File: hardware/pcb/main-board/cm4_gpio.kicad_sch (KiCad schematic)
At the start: 14 parts, among them J402 CM4Lite SD Card, U402 RT9742SNGV

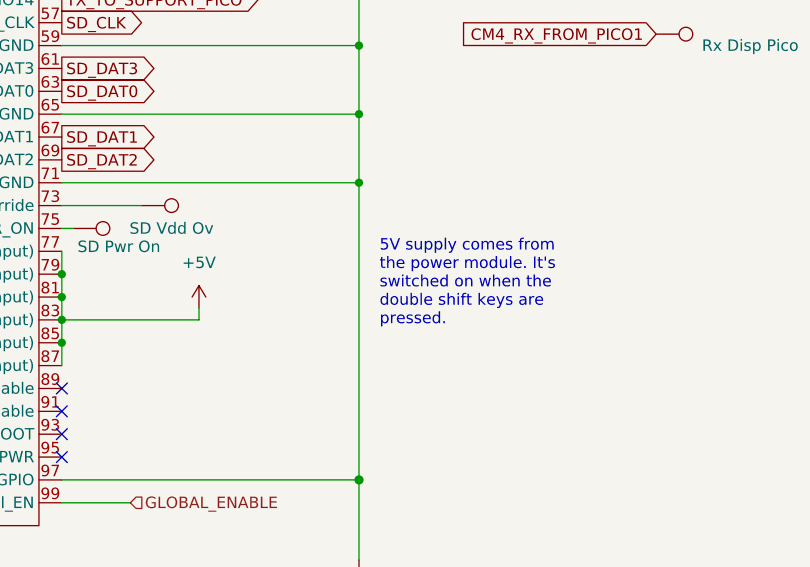
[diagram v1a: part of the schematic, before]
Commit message: CM4 power switch
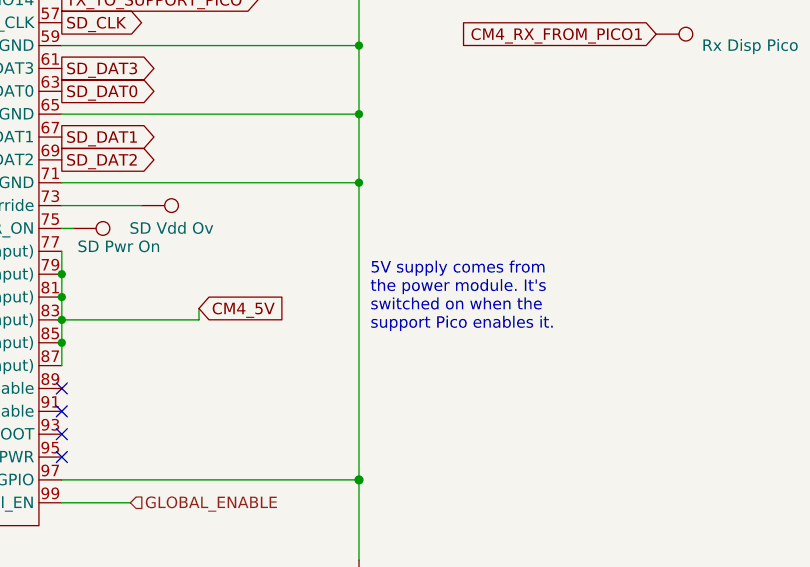
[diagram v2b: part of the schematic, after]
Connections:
- net +5V: no longer Module301.77 (+5v_(Input)), Module301.79 (+5v_(Input)), Module301.81 (+5v_(Input)), Module301.83 (+5v_(Input)), Module301.85 (+5v_(Input)), Module301.87 (+5v_(Input))
- new net CM4_5V: Module301.77 (+5v_(Input)), Module301.79 (+5v_(Input)), Module301.81 (+5v_(Input)), Module301.83 (+5v_(Input)), Module301.85 (+5v_(Input)), Module301.87 (+5v_(Input))
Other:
- note added: "5V supply comes from the power module. It's switched on when the support Pico enables it."
- note removed: "5V supply comes from the power module. It's switched on when the double shift keys are pressed."
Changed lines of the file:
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@@
 		)
 	)
-	(text "5V supply comes from\nthe power module. It's\nswitched on when the\ndouble shift keys are\npressed."
+	(text "5V supply comes from\nthe power module. It's\nswitched on when the\nsupport Pico enables it."
 		(exclude_from_sim no)
-		(at 141.986 130.556 0)
+		(at 140.97 132.08 0)
 		(effects
 			(font
@@
 		(property "Intersheetrefs" "${INTERSHEET_REFS}"
 			(at 120.9853 68.58 0)
+			(effects
+				(font
+					(size 1.27 1.27)
+				)
+				(justify left)
+				(hide yes)
+			)
+		)
+	)
+	(global_label "CM4_5V"
+		(shape input)
+		(at 121.92 133.35 0)
+		(fields_autoplaced yes)
+		(effects
+			(font
+				(size 1.27 1.27)
+			)
+			(justify left)
+		)
+		(property "Intersheetrefs" "${INTERSHEET_REFS}"
+			(at 131.4476 133.35 0)
 			(effects
 				(font
@@
 					(unit 1)
 				)
-			)
-		)
-	)
-	(symbol
-		(lib_id "power:+5V")
-		(at 121.92 133.35 0)
-		(unit 1)
-		(exclude_from_sim no)
-		(in_bom yes)
-		(on_board yes)
-		(dnp no)
-		(fields_autoplaced yes)
-		(property "Reference" "#PWR0402"
-			(at 121.92 137.16 0)
-			(effects
-				(font
-					(size 1.27 1.27)
-				)
-				(hide yes)
-			)
-		)
-		(property "Value" "+5V"
-			(at 121.92 128.27 0)
-			(effects
-				(font
-					(size 1.27 1.27)
-				)
-			)
-		)
-		(property "Footprint" ""
-			(at 121.92 133.35 0)
-			(effects
-				(font
-					(size 1.27 1.27)
-				)
-				(hide yes)
-			)
-		)
-		(property "Datasheet" ""
-			(at 121.92 133.35 0)
-			(effects
-				(font
-					(size 1.27 1.27)
-				)
-				(hide yes)
-			)
-		)
-		(property "Description" "Power symbol creates a global label with name \"+5V\""
-			(at 121.92 133.35 0)
-			(effects
-				(font
-					(size 1.27 1.27)
-				)
-				(hide yes)
-			)
-		)
-		(pin "1"
-		)
-		(instances
-			(project ""
-				(path "/fdce8012-5f35-4f58-8abb-80214b4af8fe/cd15a5fd-9317-456a-844b-3d9269d12c2d"
-					(reference "#PWR0402")
-					(unit 1)
-				)

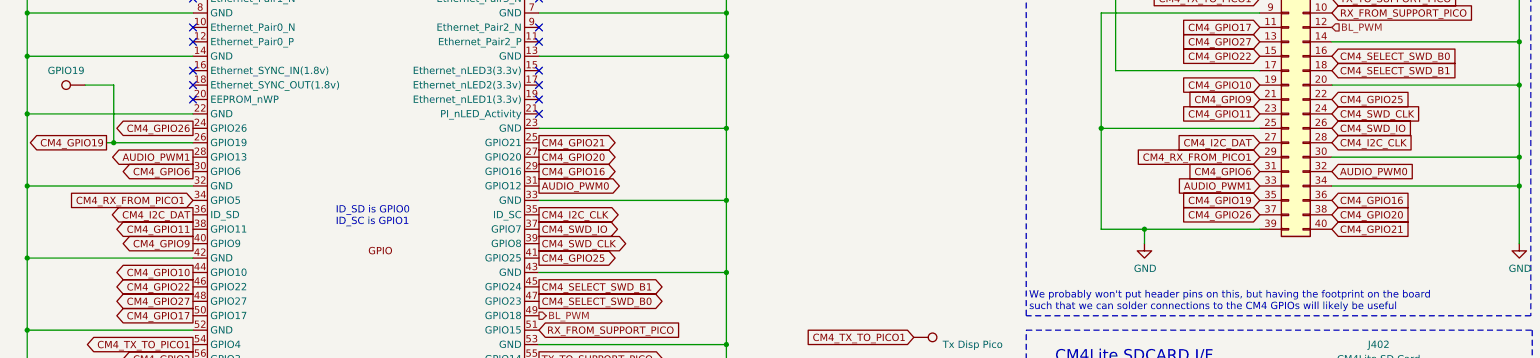
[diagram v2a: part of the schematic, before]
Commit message: add i2c connection to the support pico so it can control the RTC
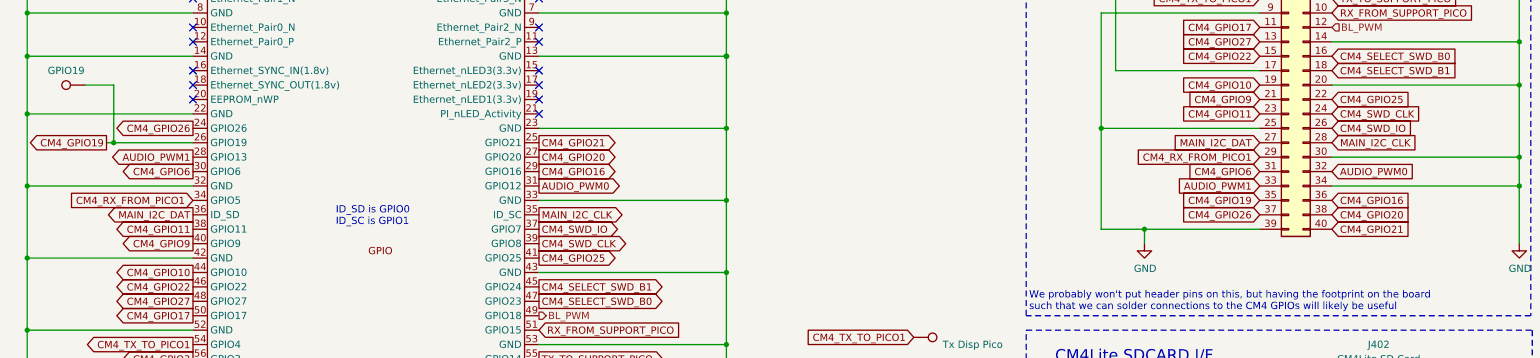
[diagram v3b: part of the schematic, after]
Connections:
- net CM4_I2C_CLK renamed MAIN_I2C_CLK
- net CM4_I2C_DAT renamed MAIN_I2C_DAT
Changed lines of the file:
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@@
 		)
 	)
-	(global_label "CM4_I2C_CLK"
+	(global_label "MAIN_I2C_CLK"
 		(shape input)
 		(at 246.38 60.96 0)
@@
 		)
 		(property "Intersheetrefs" "${INTERSHEET_REFS}"
-			(at 261.2295 60.96 0)
+			(at 261.7739 60.96 0)
 			(effects
 				(font
@@
 		)
 	)
-	(global_label "CM4_I2C_CLK"
+	(global_label "MAIN_I2C_CLK"
 		(shape output)
 		(at 106.68 73.66 0)
@@
 		)
 		(property "Intersheetrefs" "${INTERSHEET_REFS}"
-			(at 121.5295 73.66 0)
-			(effects
-				(font
-					(size 1.27 1.27)
-				)
-				(justify left)
-				(hide yes)
-			)
-		)
-	)
-	(global_label "CM4_I2C_DAT"
+			(at 122.0739 73.66 0)
+			(effects
+				(font
+					(size 1.27 1.27)
+				)
+				(justify left)
+				(hide yes)
+			)
+		)
+	)
+	(global_label "MAIN_I2C_DAT"
 		(shape output)
 		(at 45.72 73.66 180)
@@
 		)
 		(property "Intersheetrefs" "${INTERSHEET_REFS}"
-			(at 31.1124 73.66 0)
+			(at 30.568 73.66 0)
 			(effects
 				(font
@@
 		)
 	)
-	(global_label "CM4_I2C_DAT"
+	(global_label "MAIN_I2C_DAT"
 		(shape input)
 		(at 233.68 60.96 180)
@@
 		)
 		(property "Intersheetrefs" "${INTERSHEET_REFS}"
-			(at 219.0724 60.96 0)
-			(effects
-				(font
+			(at 218.528 60.96 0)
+			(effects
+				(font

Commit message: make a start on RP2040 to replace the KB pico
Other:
- title: Z88R - Z88 Recreated -> Z88R - Z88 Recreation
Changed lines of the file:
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@@
 	(paper "A4")
 	(title_block
-		(title "Z88R - Z88 Recreated")
-		(date "2025-12-19")
-		(rev "20251219WIP")
+		(title "Z88R - Z88 Recreation")
+		(date "2025-12-30")
+		(rev "20251230WIP")
 		(company "Fountain and Menadue")
 	)

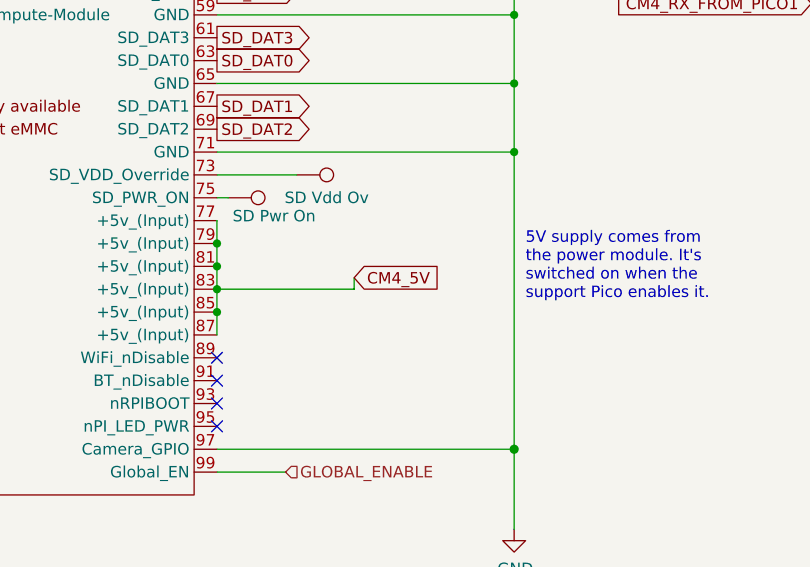
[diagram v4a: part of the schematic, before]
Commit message: start the support pico rp2040 replacement
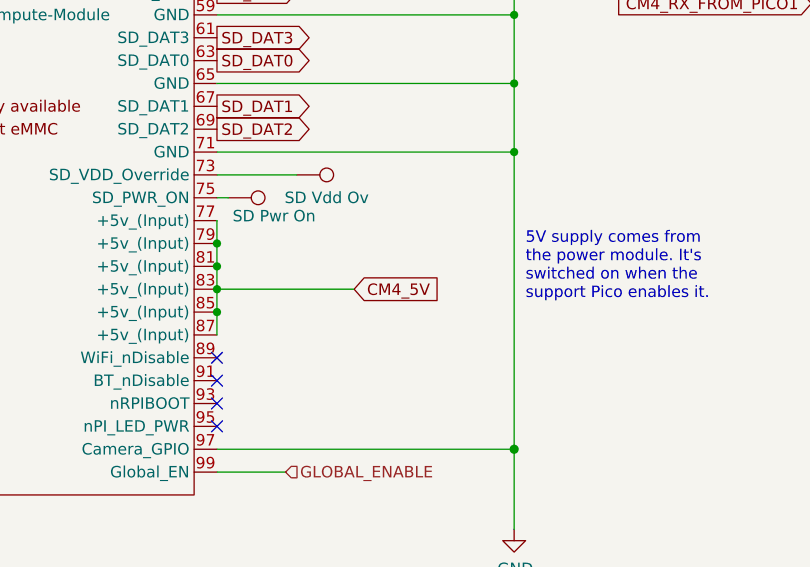
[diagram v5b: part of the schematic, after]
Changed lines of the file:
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@@
 	(title_block
 		(title "Z88R - Z88 Recreation")
-		(date "2025-12-30")
-		(rev "20251230WIP")
+		(date "2026-01-01")
+		(rev "20260101WIP")
 		(company "Fountain and Menadue")
 	)
@@
 			(width 0)
 			(type solid)
-		)
-	)
-	(wire
-		(pts
-			(xy 121.92 134.62) (xy 121.92 133.35)
-		)
-		(stroke
-			(width 0)
-			(type default)
 		)
 	)
@@
 	(global_label "CM4_5V"
 		(shape input)
-		(at 121.92 133.35 0)
+		(at 121.92 134.62 0)
 		(fields_autoplaced yes)
 		(effects
@@
 		)
 		(property "Intersheetrefs" "${INTERSHEET_REFS}"
-			(at 131.4476 133.35 0)
+			(at 131.4476 134.62 0)
 			(effects
 				(font

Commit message: more support rp2040 cleanups
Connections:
- net RX_FROM_SUPPORT_PICO renamed RX_FROM_SP_RP
- net TX_TO_SUPPORT_PICO renamed TX_TO_SP_RP
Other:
- note added: "5V supply comes from the power module. It's switched on when the support RP2040 enables it."
- note removed: "5V supply comes from the power module. It's switched on when the support Pico enables it."
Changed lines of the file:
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@@
 		)
 	)
-	(text "5V supply comes from\nthe power module. It's\nswitched on when the\nsupport Pico enables it."
+	(text "5V supply comes from\nthe power module. It's\nswitched on when the\nsupport RP2040 enables it."
 		(exclude_from_sim no)
 		(at 140.97 132.08 0)
@@
 		)
 	)
-	(global_label "RX_FROM_SUPPORT_PICO"
+	(global_label "RX_FROM_SP_RP"
 		(shape input)
 		(at 106.68 93.98 0)
@@
 		)
 		(property "Intersheetrefs" "${INTERSHEET_REFS}"
-			(at 132.6572 93.98 0)
+			(at 124.5533 93.98 0)
 			(effects
 				(font
@@
 		)
 	)
-	(global_label "RX_FROM_SUPPORT_PICO"
+	(global_label "RX_FROM_SP_RP"
 		(shape input)
 		(at 246.38 38.1 0)
@@
 		)
 		(property "Intersheetrefs" "${INTERSHEET_REFS}"
-			(at 272.3572 38.1 0)
+			(at 264.2533 38.1 0)
 			(effects
 				(font
@@
 		)
 	)
-	(global_label "TX_TO_SUPPORT_PICO"
+	(global_label "TX_TO_SP_RP"
 		(shape input)
 		(at 246.38 35.56 0)
@@
 		)
 		(property "Intersheetrefs" "${INTERSHEET_REFS}"
-			(at 269.2124 35.56 0)
+			(at 261.1085 35.56 0)
 			(effects
 				(font
@@
 		)
 	)
-	(global_label "TX_TO_SUPPORT_PICO"
+	(global_label "TX_TO_SP_RP"
 		(shape output)
 		(at 106.68 99.06 0)
@@
 		)
 		(property "Intersheetrefs" "${INTERSHEET_REFS}"
-			(at 129.5124 99.06 0)
-			(effects
-				(font
+			(at 121.4085 99.06 0)
+			(effects
+				(font

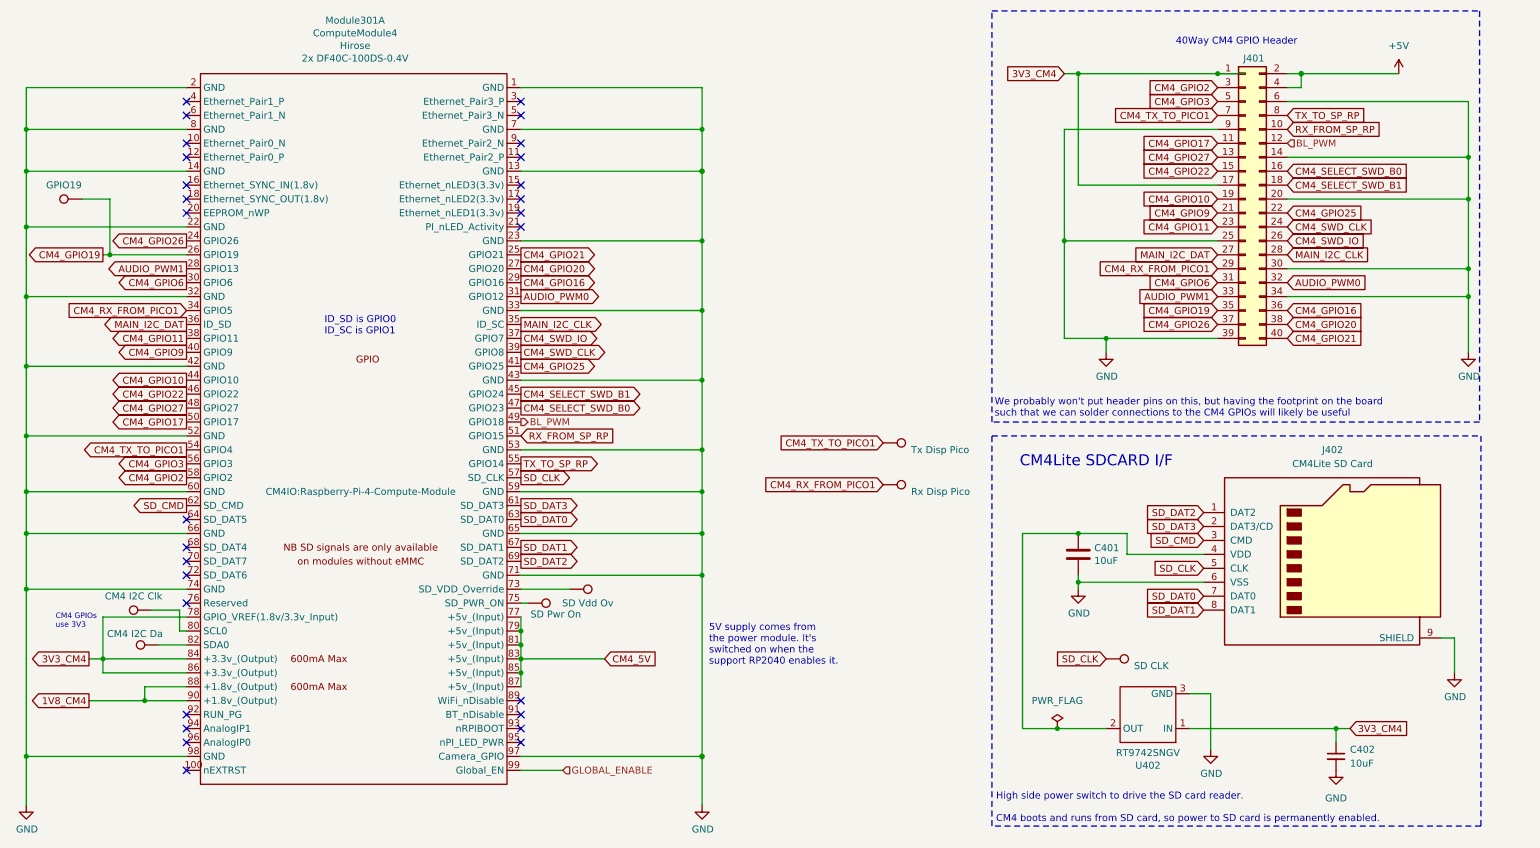
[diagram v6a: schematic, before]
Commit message: rename display board things to application board things
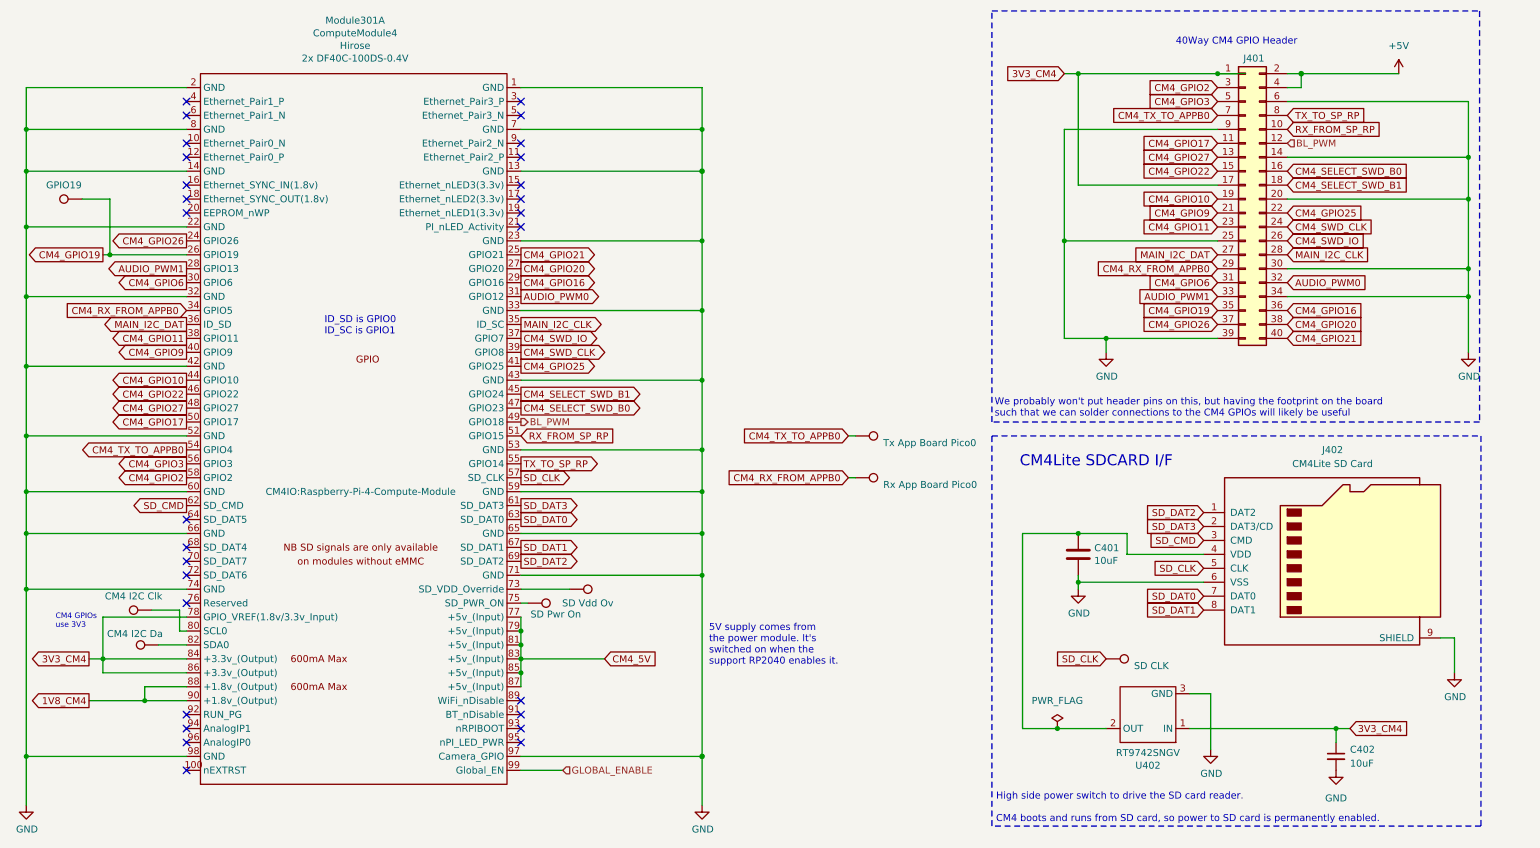
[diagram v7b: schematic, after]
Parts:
- TP408: value Tx Disp Pico -> Tx App Board Pico0
- TP409: value Rx Disp Pico -> Rx App Board Pico0
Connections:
- net CM4_RX_FROM_PICO1 renamed CM4_RX_FROM_APPB0
- net CM4_TX_TO_PICO1 renamed CM4_TX_TO_APPB0
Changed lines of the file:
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@@
 	(wire
 		(pts
+			(xy 167.64 93.98) (xy 166.37 93.98)
+		)
+		(stroke
+			(width 0)
+			(type default)
+		)
+	)
+	(wire
+		(pts
 			(xy 106.68 104.14) (xy 139.7 104.14)
 		)
@@
 	(wire
 		(pts
+			(xy 167.64 101.6) (xy 166.37 101.6)
+		)
+		(stroke
+			(width 0)
+			(type default)
+		)
+	)
+	(wire
+		(pts
 			(xy 106.68 38.1) (xy 139.7 38.1)
 		)
@@
 		)
 	)
-	(global_label "CM4_TX_TO_PICO1"
+	(global_label "CM4_TX_TO_APPB0"
 		(shape output)
 		(at 45.72 96.52 180)
@@
 		)
 		(property "Intersheetrefs" "${INTERSHEET_REFS}"
-			(at 26.3953 96.52 0)
+			(at 25.972 96.52 0)
 			(effects
 				(font
@@
 		)
 	)
-	(global_label "CM4_RX_FROM_PICO1"
+	(global_label "CM4_RX_FROM_APPB0"
 		(shape input)
 		(at 233.68 63.5 180)
@@
 		)
 		(property "Intersheetrefs" "${INTERSHEET_REFS}"
-			(at 211.2105 63.5 0)
+			(at 210.7872 63.5 0)
 			(effects
 				(font
@@
 		)
 	)
-	(global_label "CM4_TX_TO_PICO1"
+	(global_label "CM4_TX_TO_APPB0"
 		(shape input)
-		(at 172.72 95.25 180)
+		(at 166.37 93.98 180)
 		(fields_autoplaced yes)
 		(effects
@@
 		)
 		(property "Intersheetrefs" "${INTERSHEET_REFS}"
-			(at 153.3953 95.25 0)
+			(at 146.622 93.98 0)
 			(effects
 				(font
@@
 		)
 	)
-	(global_label "CM4_RX_FROM_PICO1"
+	(global_label "CM4_RX_FROM_APPB0"
 		(shape input)
-		(at 172.72 102.87 180)
+		(at 166.37 101.6 180)
 		(fields_autoplaced yes)
 		(effects
@@
 		)
 		(property "Intersheetrefs" "${INTERSHEET_REFS}"
-			(at 150.2505 102.87 0)
+			(at 143.4772 101.6 0)
 			(effects
 				(font
@@
 		)
 	)
-	(global_label "CM4_TX_TO_PICO1"
+	(global_label "CM4_TX_TO_APPB0"
 		(shape input)
 		(at 233.68 35.56 180)
@@
 		)
 		(property "Intersheetrefs" "${INTERSHEET_REFS}"
-			(at 214.3553 35.56 0)
+			(at 213.932 35.56 0)
 			(effects
 				(font
@@
 		)
 	)
-	(global_label "CM4_RX_FROM_PICO1"
+	(global_label "CM4_RX_FROM_APPB0"
 		(shape input)
 		(at 45.72 71.12 180)
@@
 		)
 		(property "Intersheetrefs" "${INTERSHEET_REFS}"
-			(at 23.2505 71.12 0)
+			(at 22.8272 71.12 0)
 			(effects
 				(font
@@
 	(symbol
 		(lib_id "Connector:TestPoint")
-		(at 172.72 102.87 270)
+		(at 167.64 101.6 270)
 		(unit 1)
 		(exclude_from_sim no)
@@
 		(dnp no)
 		(property "Reference" "TP409"
-			(at 173.736 100.584 90)
+			(at 168.656 99.314 90)
 			(effects
 				(font
@@
 			)
 		)
-		(property "Value" "Rx Disp Pico"
-			(at 177.8 104.1399 90)
+		(property "Value" "Rx App Board Pico0"
+			(at 172.72 102.8699 90)
 			(effects
 				(font
@@
 		)
 		(property "Footprint" "TestPoint:TestPoint_THTPad_D2.0mm_Drill1.0mm"
-			(at 172.72 107.95 0)
+			(at 167.64 106.68 0)
 			(effects
 				(font
@@
 		)
 		(property "Datasheet" "~"
-			(at 172.72 107.95 0)
+			(at 167.64 106.68 0)
 			(effects
 				(font
@@
 		)
 		(property "Description" "test point"
-			(at 172.72 102.87 0)
+			(at 167.64 101.6 0)
 			(effects
 				(font
@@
 	(symbol
 		(lib_id "Connector:TestPoint")
-		(at 172.72 95.25 270)
+		(at 167.64 93.98 270)
 		(unit 1)
 		(exclude_from_sim no)
@@
 		(dnp no)
 		(property "Reference" "TP408"
-			(at 173.736 92.964 90)
+			(at 168.656 91.694 90)
 			(effects
 				(font
@@
 			)
 		)
-		(property "Value" "Tx Disp Pico"
-			(at 177.8 96.5199 90)
+		(property "Value" "Tx App Board Pico0"
+			(at 172.72 95.2499 90)
 			(effects
 				(font
@@
 		)
 		(property "Footprint" "TestPoint:TestPoint_THTPad_D2.0mm_Drill1.0mm"
-			(at 172.72 100.33 0)
+			(at 167.64 99.06 0)
 			(effects
 				(font
@@
 		)
 		(property "Datasheet" "~"
-			(at 172.72 100.33 0)
+			(at 167.64 99.06 0)
 			(effects
 				(font
@@
 		)
 		(property "Description" "test point"
-			(at 172.72 95.25 0)
+			(at 167.64 93.98 0)
 			(effects
 				(font
